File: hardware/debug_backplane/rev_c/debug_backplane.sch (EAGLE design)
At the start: 322 parts, among them J1 BACKPLANE_CONTROLLER_MODULE_D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, J11 PJ-102AH, J12 MICRO_USB_B_HIROSE_ZX62R-B-5P, J2 BACKPLANE_GENERIC_MODULE_DEBUG, J3 BACKPLANE_GENERIC_MODULE_DEBUG, J4 TC2030-FTDI-I2C, J9 MICRO_USB_B_HIROSE_ZX62R-B-5P, Q1 DMN32D2LDF, Q10 MOSFET-NCHANNELSMD, Q2 DMN32D2LDF, Q3 DMN32D2LDF, Q4 DMN32D2LDF, Q5 DMN32D2LDF, Q6 DMN32D2LDF, Q7 DMN32D2LDF, U1 FT232RQ, U10 LTC2943, U11 LTC2943, U12 MAX8887EZK33+T, U13 MCP23008QFN, U14 MCP23008QFN, U15 PCA9544AQFN-N20, U16 SAM4LC8AA, U17 SN74LVC2T45, U18 SN74LVC2T45, U19 SN74LVC2T45, U2 FT232RQ, U20 SN74LVC2T45, U21 TS3USB30E, U22 TS3USB30E, U23 TS3USB30E, U24 TUSB2077A, U25 LTC4360, U26 TUSB2077A, U27 FT232RQ, U28 MCP23008QFN, U29 M24C01WMN, U3 FT232RQ, U30 MAX6746, U31 NCP301LSN30, U32 NCP301LSN30, U4 FT232RQ, U5 FT232RQ, U6 FXMA2102, U7 FXMA2102, U8 LTC2941, U9 LTC2943, X1 16MHz, Y1 ABMM, Y2 ABMM

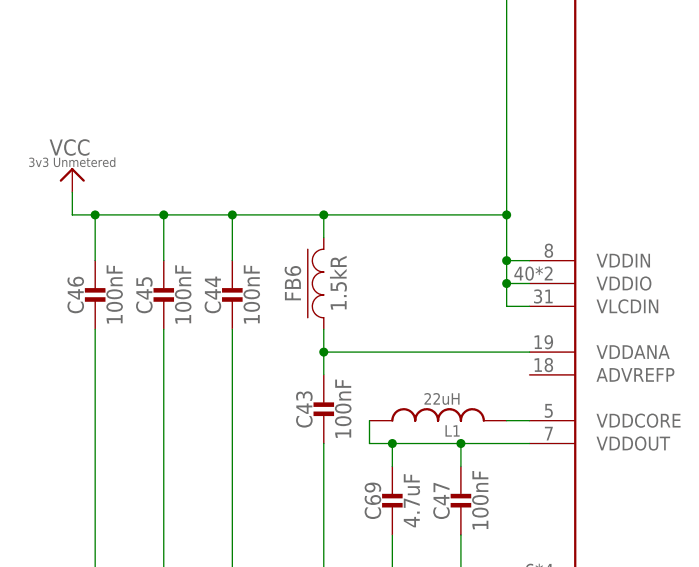
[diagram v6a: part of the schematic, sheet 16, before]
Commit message: debug_backplane: FB6 -> FB1
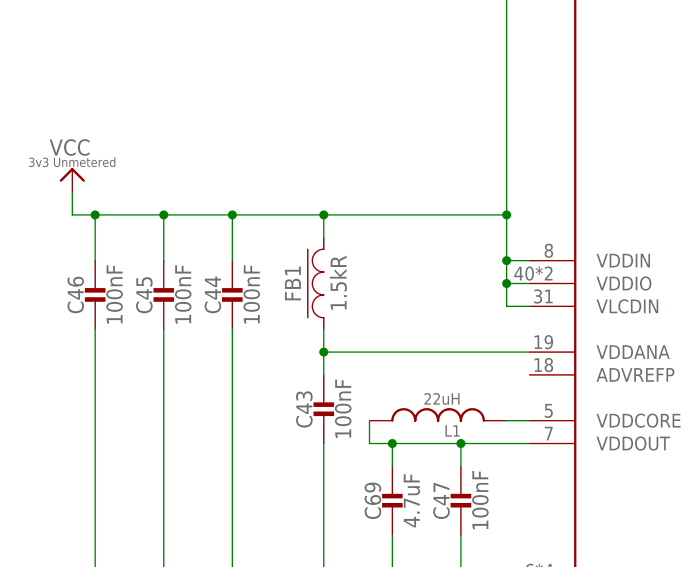
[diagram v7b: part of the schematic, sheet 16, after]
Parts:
- renumbered FB6 to FB1
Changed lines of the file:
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@@
 <attribute name="DIGIKEY" value="490-10777-1-ND"/>
 </part>
-<part name="FB6" library="passives" deviceset="FERRITE_BEAD" device="0603" value="1.5kR">
+<part name="FB1" library="passives" deviceset="FERRITE_BEAD" device="0603" value="1.5kR">
 <attribute name="DIGIKEY" value="490-5216-1-ND"/>
 </part>
@@
 <attribute name="DIGIKEY" x="10.16" y="129.54" size="1.27" layer="96" align="bottom-center" display="off"/>
 </instance>
-<instance part="FB6" gate="G$1" x="35.56" y="129.54" rot="R90">
+<instance part="FB1" gate="G$1" x="35.56" y="129.54" rot="R90">
 <attribute name="DIGIKEY" x="35.56" y="129.54" size="1.27" layer="96" font="vector" rot="R90" display="off"/>
 </instance>
@@
 <wire x1="35.56" y1="119.38" x2="35.56" y2="121.92" width="0.1524" layer="91"/>
 <junction x="35.56" y="121.92"/>
-<pinref part="FB6" gate="G$1" pin="P$1"/>
+<pinref part="FB1" gate="G$1" pin="P$1"/>
 <wire x1="35.56" y1="124.46" x2="35.56" y2="121.92" width="0.1524" layer="91"/>
 <pinref part="U16" gate="U1" pin="VDDANA"/>
@@
 <wire x1="25.4" y1="132.08" x2="25.4" y2="137.16" width="0.1524" layer="91"/>
 <junction x="25.4" y="137.16"/>
-<pinref part="FB6" gate="G$1" pin="P$2"/>
+<pinref part="FB1" gate="G$1" pin="P$2"/>
 <wire x1="35.56" y1="137.16" x2="35.56" y2="134.62" width="0.1524" layer="91"/>
 <junction x="35.56" y="137.16"/>

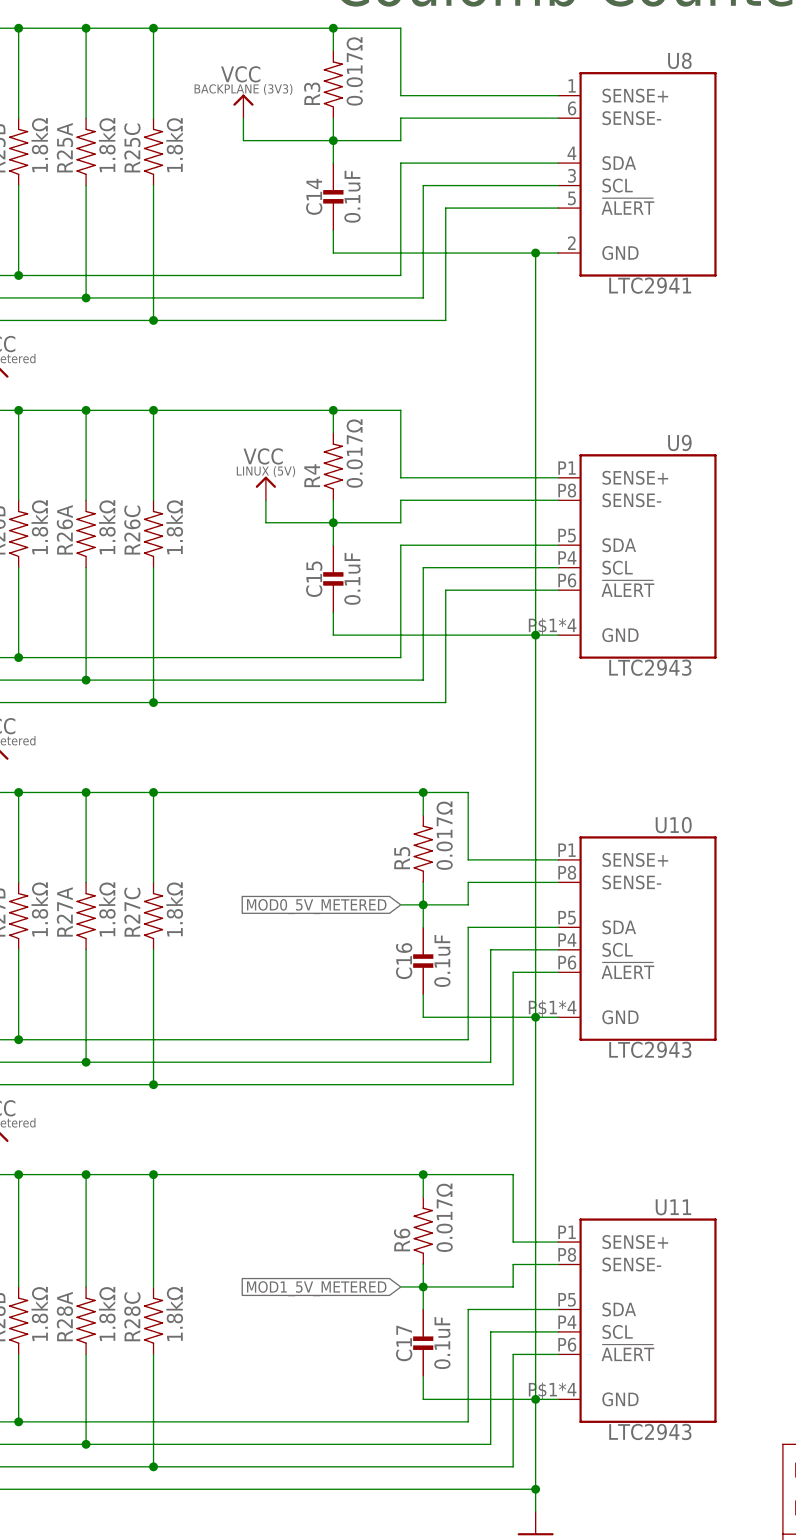
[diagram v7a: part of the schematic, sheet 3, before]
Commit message: debug_backplane: 0.1uF -> 100nF consistency
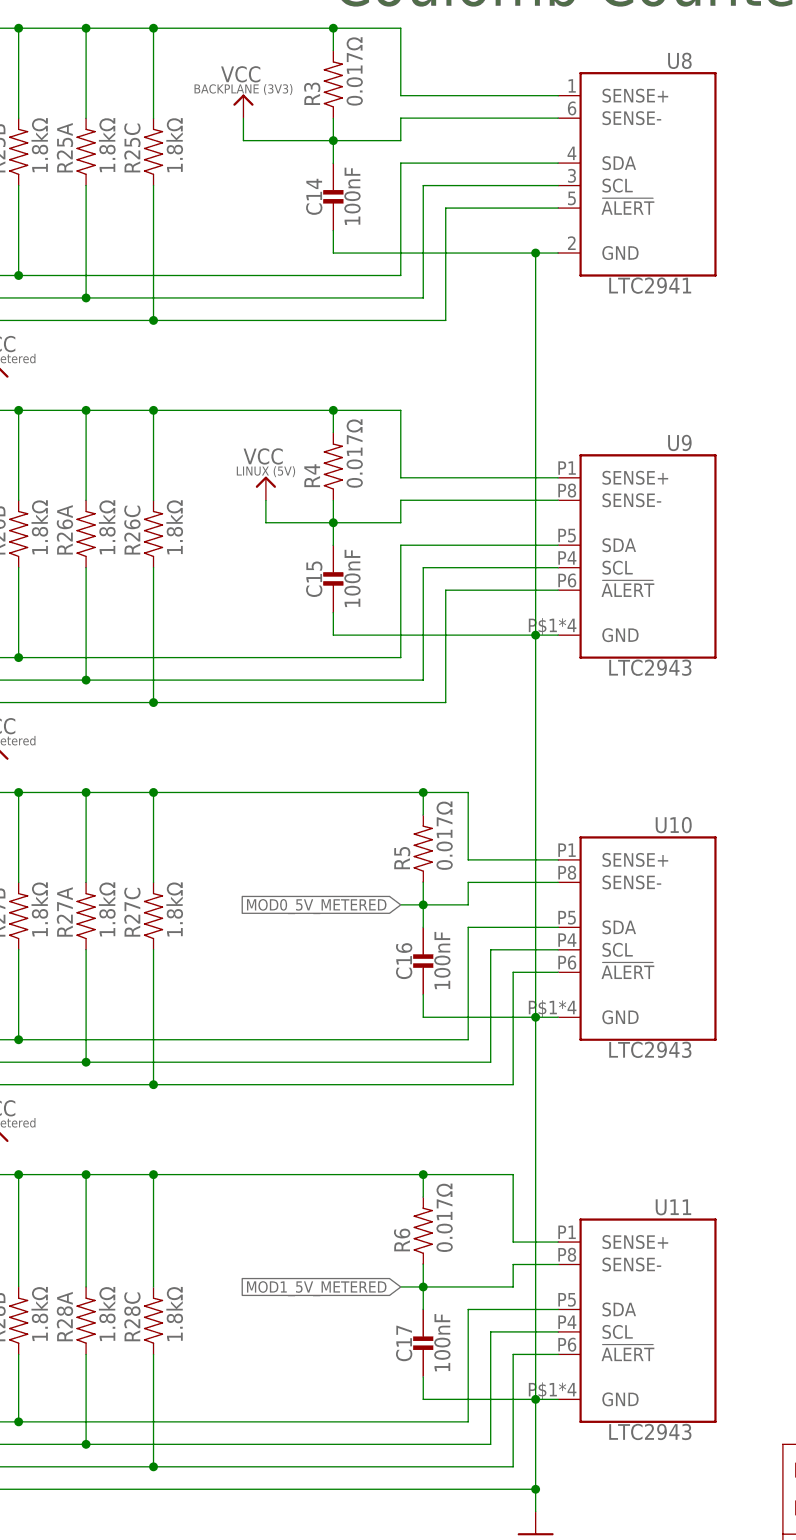
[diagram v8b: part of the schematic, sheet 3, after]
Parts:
- C14, C15, C16, C17: value 0.1uF -> 100nF
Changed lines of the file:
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@@
 </part>
 <part name="C13" library="passives" deviceset="CAPACITOR" device="0603_CAP" value="0.01uF"/>
-<part name="C14" library="passives" deviceset="CAPACITOR" device="0603_CAP" value="0.1uF"/>
-<part name="C15" library="passives" deviceset="CAPACITOR" device="0603_CAP" value="0.1uF"/>
-<part name="C16" library="passives" deviceset="CAPACITOR" device="0603_CAP" value="0.1uF"/>
-<part name="C17" library="passives" deviceset="CAPACITOR" device="0603_CAP" value="0.1uF"/>
+<part name="C14" library="passives" deviceset="CAPACITOR" device="0603_CAP" value="100nF"/>
+<part name="C15" library="passives" deviceset="CAPACITOR" device="0603_CAP" value="100nF"/>
+<part name="C16" library="passives" deviceset="CAPACITOR" device="0603_CAP" value="100nF"/>
+<part name="C17" library="passives" deviceset="CAPACITOR" device="0603_CAP" value="100nF"/>
 <part name="U$23" library="signpost" deviceset="VCC_3V3_UNMETERED" device=""/>
 <part name="U$69" library="signpost" deviceset="VCC_3V3_UNMETERED" device=""/>
